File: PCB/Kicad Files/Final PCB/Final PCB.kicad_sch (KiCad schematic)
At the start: 54 parts, among them J1 Conn_01x20_Socket, J10 Conn_01x02_Socket, J11 Conn_01x02_Socket, J12 Conn_01x02_Socket, J13 Conn_01x02_Socket, J14 Conn_01x02_Socket, J15 Conn_01x02_Socket, J16 Conn_01x02_Socket, J17 Conn_01x02_Socket, J18 Conn_01x02_Socket, J19 Conn_01x02_Socket, J5 Conn_01x02_Socket, J6 Conn_01x02_Socket, J7 Conn_01x02_Socket, J8 Conn_01x02_Socket, J9 Conn_01x02_Socket, U1 4049, U2 4049, U3 4049, U6 ESP32-DEVKIT-V1

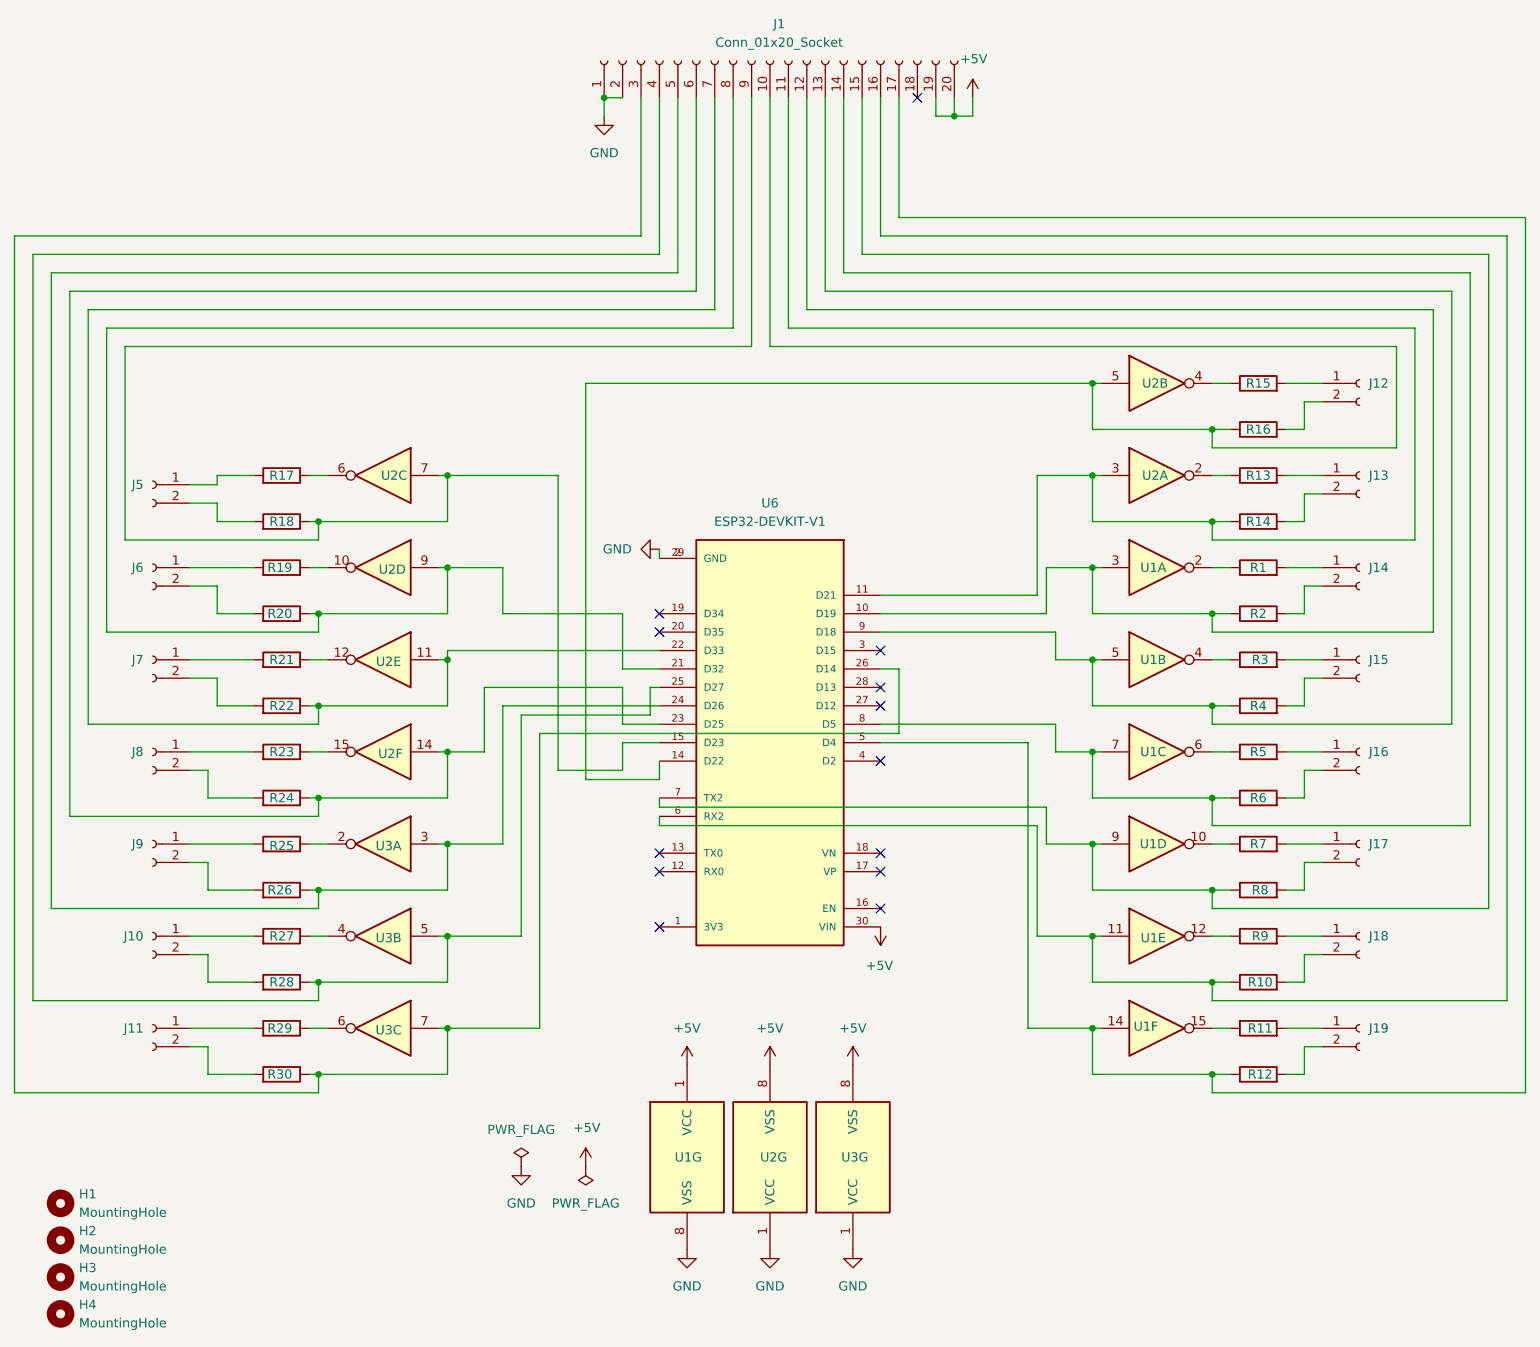
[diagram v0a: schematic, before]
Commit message: REFATORE: PCB altered with no CI 4049
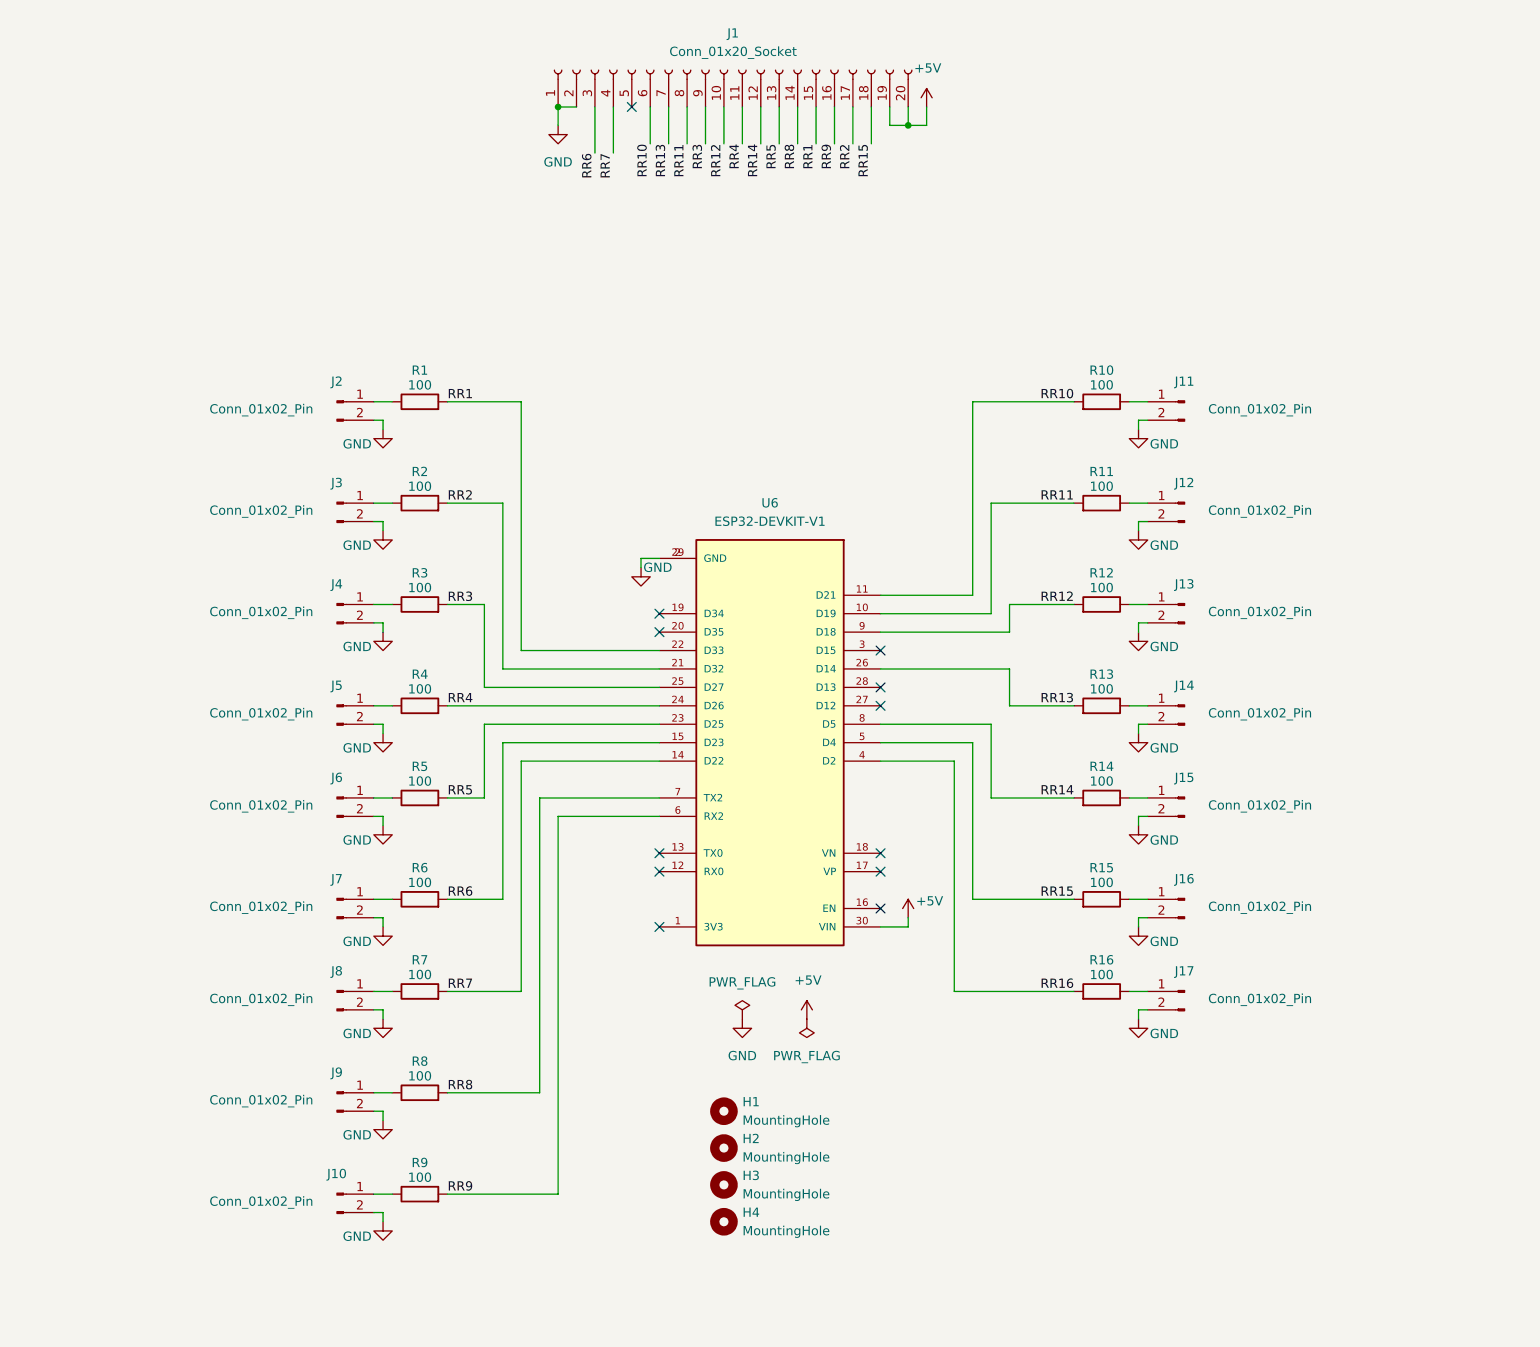
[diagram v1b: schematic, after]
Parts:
- removed J10, J11, J12, J13, J14, J15, J16, J17, J18, J19, J5, J6, J7, J8, J9: Conn_01x02_Socket, Addlibrary:PinHeader_1x02_P2.54mm_VerticalLongPads, symbol Connector:Conn_01x02_Socket
- removed R17, R18, R19, R20, R21, R22, R23, R24, R25, R26, R27, R28, R29, R30: R, Addlibrary:R_Axial_DIN0411_L9.9mm_D3.6mm_P25.40mm_HorizontalLongPads, symbol Device:R
- removed U1, U2, U3: 4049, Addlibrary:DIP-16_W7.62mm_Socket_LongPads, symbol 4xxx:4049
- added J10, J11, J12, J13, J14, J15, J16, J17, J2, J3, J4, J5, J6, J7, J8, J9: Conn_01x02_Pin, Addlibrary:PinHeader_1x02_P2.54mm_VerticalLongPads, symbol Connector:Conn_01x02_Pin
- R1, R10, R11, R12, R13, R14, R15, R16, R2, R3, R4, R5, R6, R7, R8, R9: value R -> 100; footprint Addlibrary:R_Axial_DIN0411_L9.9mm_D3.6mm_P25.40mm_HorizontalLongPads -> Addlibrary:R_Axial_DIN0411_L9.9mm_D3.6mm_P12.70mm_HorizontalLONGPADS
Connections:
- net GND: now also J10.2 (Pin_2), J11.2 (Pin_2), J12.2 (Pin_2), J13.2 (Pin_2), J14.2 (Pin_2), J15.2 (Pin_2), J16.2 (Pin_2), J17.2 (Pin_2), J2.2 (Pin_2), J3.2 (Pin_2), J4.2 (Pin_2), J5.2 (Pin_2), J6.2 (Pin_2), J7.2 (Pin_2), J8.2 (Pin_2), J9.2 (Pin_2)
- net RR16: now reaches R16.2
- net RR16: now also U6.4 (D2)
- net RR3: now reaches U6.25 (D27)
- net RR3: now also J1.9 (Pin_9), R3.2; no longer J1.4 (Pin_4)
- net at R7.1: now also J8.1 (Pin_1)
- net RR13: now reaches U6.26 (D14)
- net RR13: now also J1.7 (Pin_7), R13.2; no longer J1.3 (Pin_3)
- net at J1.5 (Pin_5): no longer U6.24 (D26)
- net at R9.1: now also J10.1 (Pin_1)
- net RR9: now reaches R9.2
- net RR9: now also J1.16 (Pin_16), U6.6 (RX2)
- net RR4: now reaches R4.2
- net RR4: now also J1.11 (Pin_11), U6.24 (D26)
- net RR14: now reaches R14.2
- net RR14: now also J1.12 (Pin_12), U6.8 (D5)
- net RR15: now reaches J1.18 (Pin_18)
- net RR15: now also R15.2, U6.5 (D4)
- net RR10: now reaches J1.6 (Pin_6)
- net RR10: now also R10.2, U6.11 (D21); no longer U6.23 (D25)
- net RR1: now reaches U6.22 (D33)
- net RR1: now also J1.15 (Pin_15), R1.2; no longer J1.7 (Pin_7)
- net RR11: now reaches J1.8 (Pin_8)
- net RR11: now also R11.2, U6.10 (D19); no longer U6.21 (D32)
- net RR6: now reaches U6.15 (D23)
- net RR6: now also J1.3 (Pin_3), R6.2; no longer J1.9 (Pin_9)
- net RR7: now reaches R7.2
- net RR7: now also J1.4 (Pin_4), U6.14 (D22)
- net RR8: now reaches R8.2
- net RR8: now also J1.14 (Pin_14), U6.7 (TX2)
- net RR5: now reaches R5.2
- net RR5: now also J1.13 (Pin_13), U6.23 (D25)
- net at R1.1: now also J2.1 (Pin_1)
- net at R11.1: now also J12.1 (Pin_1)
- net at R3.1: now also J4.1 (Pin_1)
- net RR2: now reaches R2.2
- net RR2: now also J1.17 (Pin_17), U6.21 (D32)
- net at R5.1: now also J6.1 (Pin_1)
- net at R13.1: now also J14.1 (Pin_1)
- net at R15.1: now also J16.1 (Pin_1)
- net RR12: now reaches R12.2
- net RR12: now also J1.10 (Pin_10), U6.9 (D18)
- new net: J9.1 (Pin_1), R8.1
- new net: J3.1 (Pin_1), R2.1
- new net: J17.1 (Pin_1), R16.1
- new net: J13.1 (Pin_1), R12.1
- new net: J15.1 (Pin_1), R14.1
- new net: J11.1 (Pin_1), R10.1
- new net: J7.1 (Pin_1), R6.1
- new net: J5.1 (Pin_1), R4.1
- no-connect marks 13 -> 12
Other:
- moved on the sheet: H1, H2, H3, H4, J1
